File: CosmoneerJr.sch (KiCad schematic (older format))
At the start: 88 parts, among them J1 Header, J12 Header, J13 Header, J16 Header, J17 Header, J18 Header, J4 Header, J5 Header, J8 Header, J9 Header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

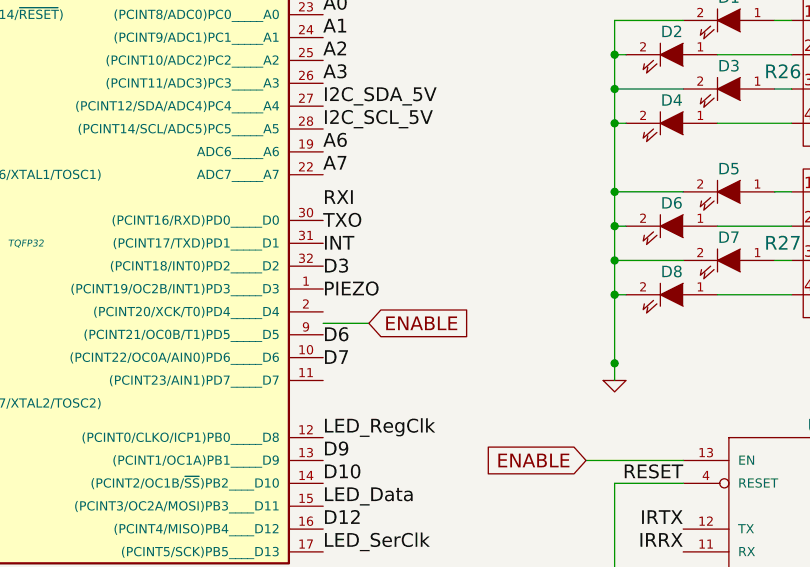
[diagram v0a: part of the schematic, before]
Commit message: PDF added
Generated a pdf version of the schematic

Schematic fixes made

Net connections on U1 were disconnected during component move.  Nets
reconnected, pdf generated, netlist generated and re-imported into pcb.
PCB file updated and saved.
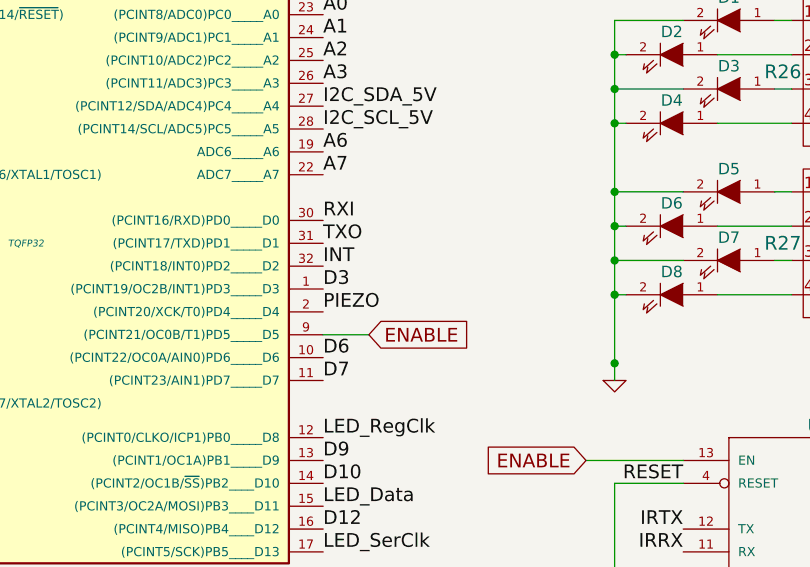
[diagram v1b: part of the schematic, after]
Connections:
- net D3: now also U1.1 ((PCINT19/OC2B/INT1)PD3_____D3)
- net D6: now also U1.10 ((PCINT22/OC0A/AIN0)PD6_____D6)
- net D7: now also U1.11 ((PCINT23/AIN1)PD7_____D7)
- net ENABLE: now also U1.9 ((PCINT21/OC0B/T1)PD5_____D5)
- net INT: now also U1.32 ((PCINT18/INT0)PD2_____D2)
- net PIEZO: now also U1.2 ((PCINT20/XCK/T0)PD4_____D4)
- net RXI: now also U1.30 ((PCINT16/RXD)PD0_____D0)
- net TXO: now also U1.31 ((PCINT17/TXD)PD1_____D1)
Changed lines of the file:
@@
 Sheet 1 1
 Title "Cosmoneer Jr Main Board"
-Date "28 jun 2014"
+Date "1 jul 2014"
 Rev "-"
 Comp "Cosmos Pioneering"
@@
 Text Label 6825 1525 2    60   ~ 0
 PIEZO
-Text Label 6450 3875 0    60   ~ 0
+Text Label 6450 3925 0    60   ~ 0
 PIEZO
 Text Label 6450 3025 0    60   ~ 0
@@
 	1    0    0    -1
 $EndComp
-Text GLabel 6650 3975 2    60   Input ~ 0
+Text GLabel 6650 4025 2    60   Input ~ 0
 ENABLE
 $Comp
@@
 	1    0    0    -1
 $EndComp
-Text Label 6450 3675 0    60   ~ 0
+Text Label 6450 3725 0    60   ~ 0
 INT
 Text Label 2075 6150 1    60   ~ 0
@@
 	-1   0    0    1
 $EndComp
-Text Label 6450 3475 0    60   ~ 0
+Text Label 6450 3525 0    60   ~ 0
 RXI
-Text Label 6450 3575 0    60   ~ 0
+Text Label 6450 3625 0    60   ~ 0
 TXO
 Text Label 4550 4725 2    60   ~ 0
@@
 Text Label 6450 2625 0    60   ~ 0
 A0
-Text Label 6450 3775 0    60   ~ 0
+Text Label 6450 3825 0    60   ~ 0
 D3
-Text Label 6450 4075 0    60   ~ 0
+Text Label 6450 4125 0    60   ~ 0
 D6
-Text Label 6450 4175 0    60   ~ 0
+Text Label 6450 4225 0    60   ~ 0
 D7
 Text Label 6450 4575 0    60   ~ 0
@@
 	8025 4575 7600 4575
 Wire Wire Line
-	6450 3975 6650 3975
+	6450 4025 6650 4025
 Wire Wire Line
 	2275 7550 2525 7550

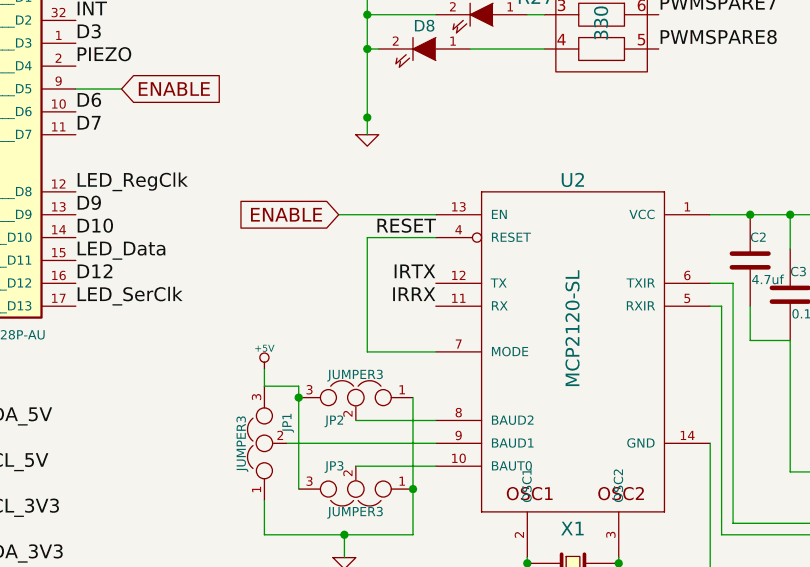
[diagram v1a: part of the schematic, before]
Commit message: Pressfit PCB additions
Added pads, drills and Silkscreen outlines for press fit pcb additions.
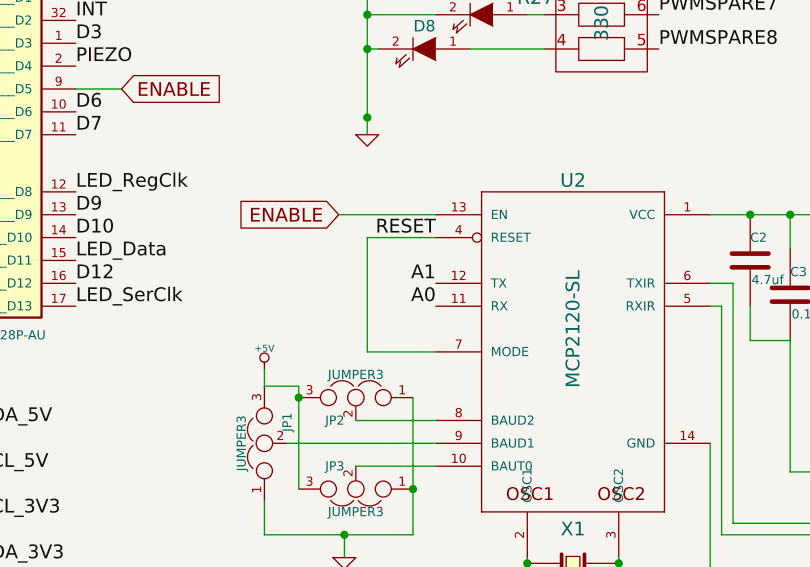
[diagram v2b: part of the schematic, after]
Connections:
- net IRRX is gone; now on net A0: U2.11 (RX)
- net IRTX is gone; now on net A1: U2.12 (TX)
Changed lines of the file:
@@
 Sheet 1 1
 Title "Cosmoneer Jr Main Board"
-Date "1 jul 2014"
+Date "13 jul 2014"
 Rev "-"
 Comp "Cosmos Pioneering"
@@
 $EndComp
 Text Label 8025 4875 2    60   ~ 0
-IRTX
+A1
 Text Label 8025 4975 2    60   ~ 0
-IRRX
+A0
 Text Label 8025 4675 2    60   ~ 0
 RESET

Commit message: Final changes
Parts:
- removed J12, J16, J4, J8: Header, symbol CONN_3
- removed R1, R2, R3, R4, R5, R6: 0 Ohm, ~, symbol R
- removed R10, R11, R12, R13, R8, R9: 10K, ~, symbol R
- added JP4, JP5: JUMPER3, ~, symbol JUMPER3
- added P7, P8: CONN_2, ~, symbol CONN_2
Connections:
- net RA2 is gone; now on net +5V: U9.3 (A2)
- net RA3 is gone; now on net +5V: U9.4 (A3)
- net RA4 is gone; now on net +5V: U9.5 (A4)
- net RA5 is gone; now on net +5V: U9.24 (A5)
- net +5V: now also JP4.3, JP5.3
- net GND: now also JP4.1, JP5.1
- net RA0: now also JP4.2
- net RA1: now also JP5.2
- net at R28.1: now also P7.1 (P1)
- net at R28.2: now also P7.2 (PM)
- net at R28.3: now also P8.1 (P1)
- net at R28.4: now also P8.2 (PM)

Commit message: Rev ZeroOne Prototype
Parts added, Schematic updated and PCB updated and Mfg files generated
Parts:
- removed C10, C11: 0.1uf, ~, symbol C
- removed C8: 4.7uf, ~, symbol C
- removed C9: 0.22uf, ~, symbol C
- removed P5: Header, symbol CONN_2
- removed R20, R21, R22, R23: 10K, ~, symbol R
- removed U4: PCA9306, symbol PCA9306
- removed U5: HMC5883, symbol HMC5883
- added D11: 1N4001, diode-DO41-10, symbol 1N4004
- added F1: FUSE, symbol FUSE
- added U10: GY-271, symbol GY-271
- C13, C14: value 22pf -> 15pf
- C6, C7: value 22pf -> 27pf
- R25, R28: value 220 Ohm -> 330 Ohm
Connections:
- net labels added: +5VB
- net labels removed: +3.3V, I2C_SCL_3V3, I2C_SDA_3V3
- wire segments 195 -> 186
- no-connect marks 1 -> 0
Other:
- moved on the sheet: P6
